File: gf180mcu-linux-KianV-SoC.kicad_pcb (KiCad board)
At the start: 4 copper layers, 94.7 x 52 mm, 64 parts, among them CN1 HC-PBB40C-70DS-0.4V-2.0-02_CU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, J2 Conn_01x06_Pin, J3 Conn_01x06_Pin, J4 Conn_02x06_Top_Bottom_custom, J5 USB_C_Receptacle_PowerOnly_6P, SW1 SW_Push, U1 MT48LC16M16A2P, U2 TPS3808DBV, U3 TLV62569DBV, Y1 CXO_DIP8

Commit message: fixed sdcard
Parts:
- added J1: Micro_SD_Card, Connector_Card:microSD_HC_Molex_47219-2001, F.Cu at (167.7, 224.2)
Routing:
- net /SPI0_SCLK: track 43.0 -> 47.0 mm, vias 2 -> 3
- net GND: track 67.5 -> 69.8 mm, vias 186 -> 187
- net /SPI0_CSN: track 58.3 -> 59.5 mm, vias 2 -> 3
- net /3V3: track 488.1 -> 487.0 mm
- net /SPI1_MOSI: track 46.2 -> 45.2 mm
- net /FLASH_MISO: track 33.3 -> 32.6 mm
- net /FLASH_SCLK: track 25.0 -> 24.4 mm

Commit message: rework: silk
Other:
- board text added: "Board design review by Andrew Wingate"
- board text added: "Board design support by Goran Maholvic"
- board text added: "RTL / PCB / ASIC – H. Dabui ASIC flow & PDK support L. Moser"
- board text removed: "SoC Design: logic destroyer, ASIC design support Leo moser"
- board text removed: "board Design review by Andrew Wingate"
- board text removed: "board Design support by Goran Maholvic"
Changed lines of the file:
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@@
 	)
 	(paper "A0")
+	(title_block
+		(comment 4 "AISLER Project ID: DDGQJPWZ")
+	)
 	(layers
 		(0 "F.Cu" signal)
@@
 		)
 		(pad_to_mask_clearance 0.05)
-		(solder_mask_min_width 0.25)
 		(pad_to_paste_clearance -0.05)
 		(allow_soldermask_bridges_in_footprints yes)
@@
 		)
 	)
-	(gr_text "board Design support by\nGoran Maholvic"
+	(gr_text "Board design support by\nGoran Maholvic"
 		(at 178.37 183.32 0)
 		(layer "F.SilkS")
@@
 		)
 	)
-	(gr_text "SoC Design: logic destroyer,\nASIC design support Leo moser"
-		(at 223.88 207.6 90)
+	(gr_text "RTL / PCB / ASIC – H. Dabui\nASIC flow & PDK support L. Moser"
+		(at 223.88 205.7 90)
 		(layer "F.SilkS")
 		(effects
@@
 		)
 	)
-	(gr_text "board Design review by\nAndrew Wingate"
+	(gr_text "Board design review by\nAndrew Wingate"
 		(at 217.13 227.1 0)
 		(layer "B.SilkS")

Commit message: small tweaks
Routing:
- net GND: track 69.8 -> 63.4 mm, vias 187 -> 186
- net /3V3: track 487.0 -> 485.0 mm
- net /SPI0_MOSI: track 46.8 -> 48.2 mm
- net /SPI0_SCLK: track 47.0 -> 47.8 mm

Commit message: first pass complete
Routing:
- net GND: track 63.4 -> 60.0 mm, vias 186 -> 192
- net /3V3: track 485.0 -> 485.7 mm
- net /SPI1_MOSI: track 45.2 -> 45.9 mm
- net VBUS: track 12.5 -> 13.1 mm

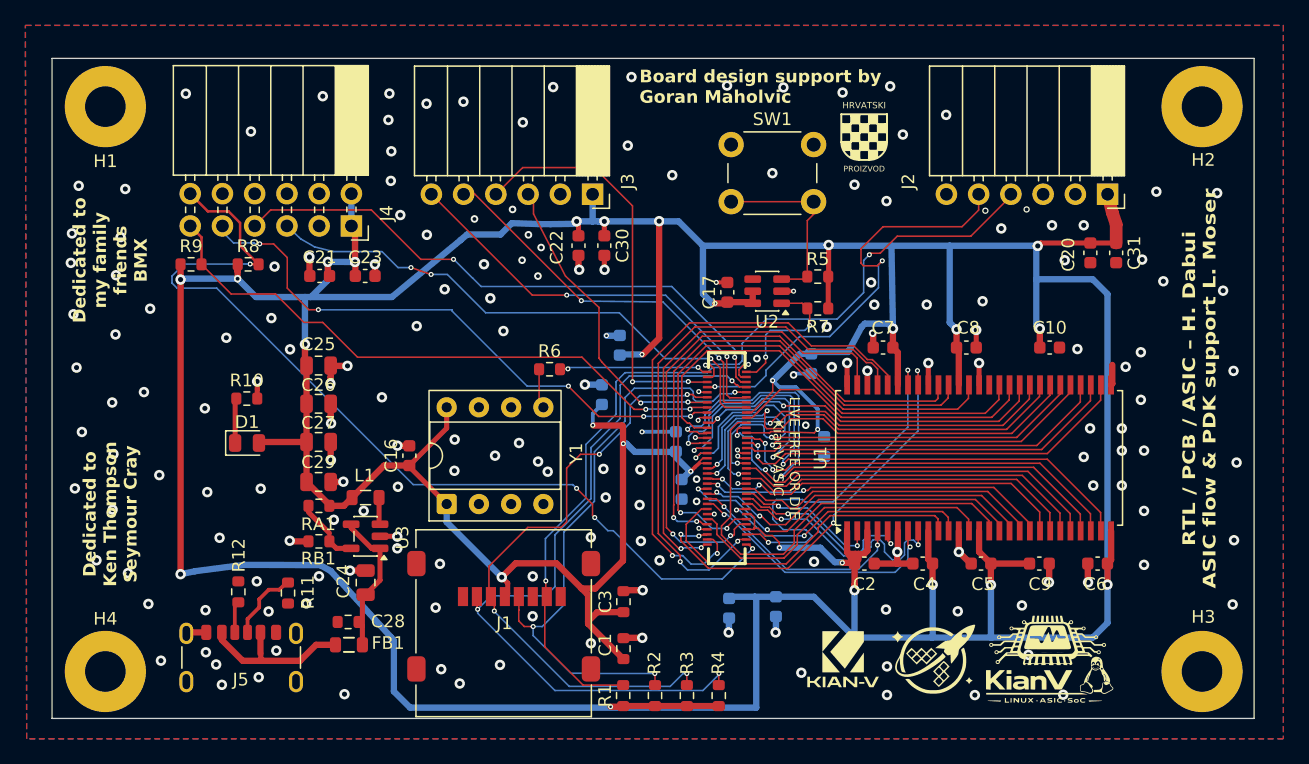
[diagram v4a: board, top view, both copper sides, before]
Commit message: rework: silk text, sdram cap gnd, power lines, ...
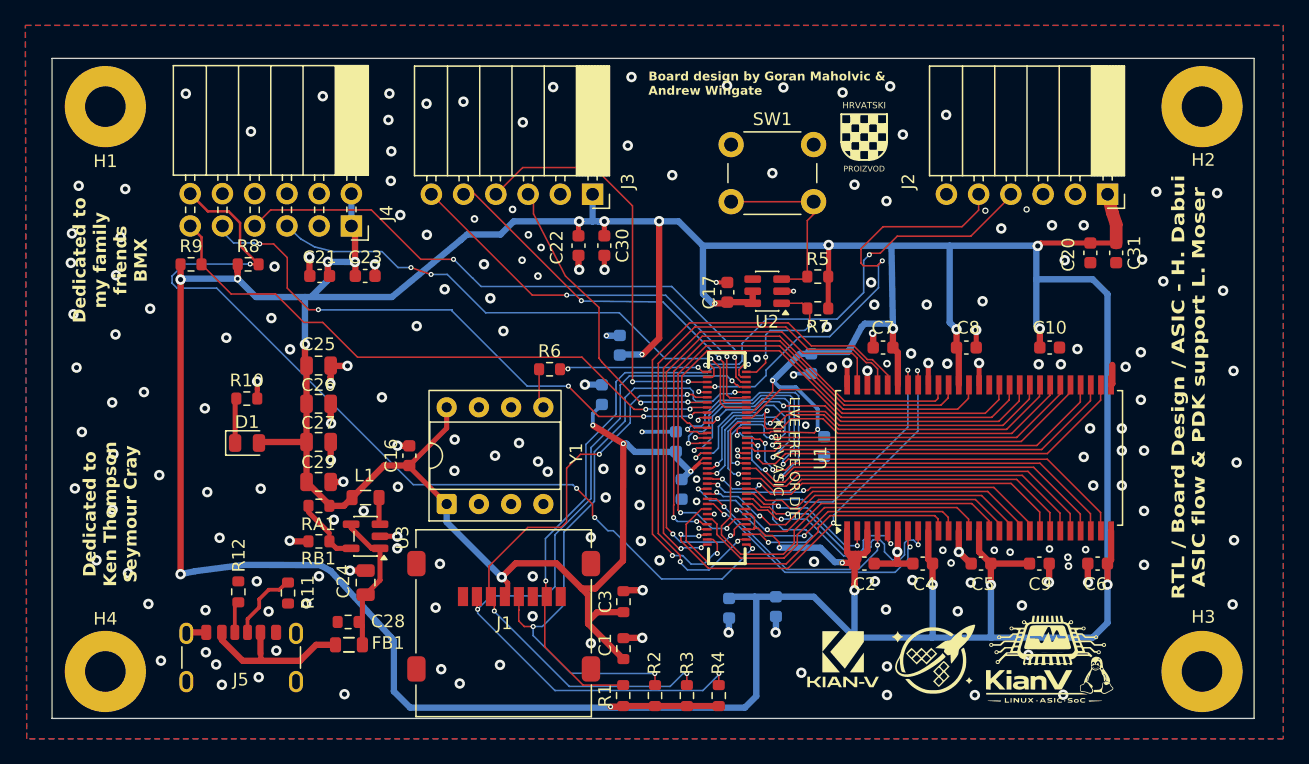
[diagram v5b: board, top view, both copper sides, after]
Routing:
- net /3V3: track 485.7 -> 483.8 mm
- net GND: vias 192 -> 208
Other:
- board text added: "Board Review by Andrew Wingate"
- board text added: "Board design by Goran Maholvic & Andrew Wingate"
- board text added: "RTL / Board Design / ASIC - H. Dabui ASIC flow & PDK support L. Moser"
- board text removed: "Board design review by Andrew Wingate"
- board text removed: "Board design support by Goran Maholvic"
- board text removed: "RTL / PCB / ASIC – H. Dabui ASIC flow & PDK support L. Moser"
